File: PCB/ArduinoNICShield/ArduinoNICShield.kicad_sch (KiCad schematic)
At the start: 4 parts, among them J2 OUT, Q1 PN2222A

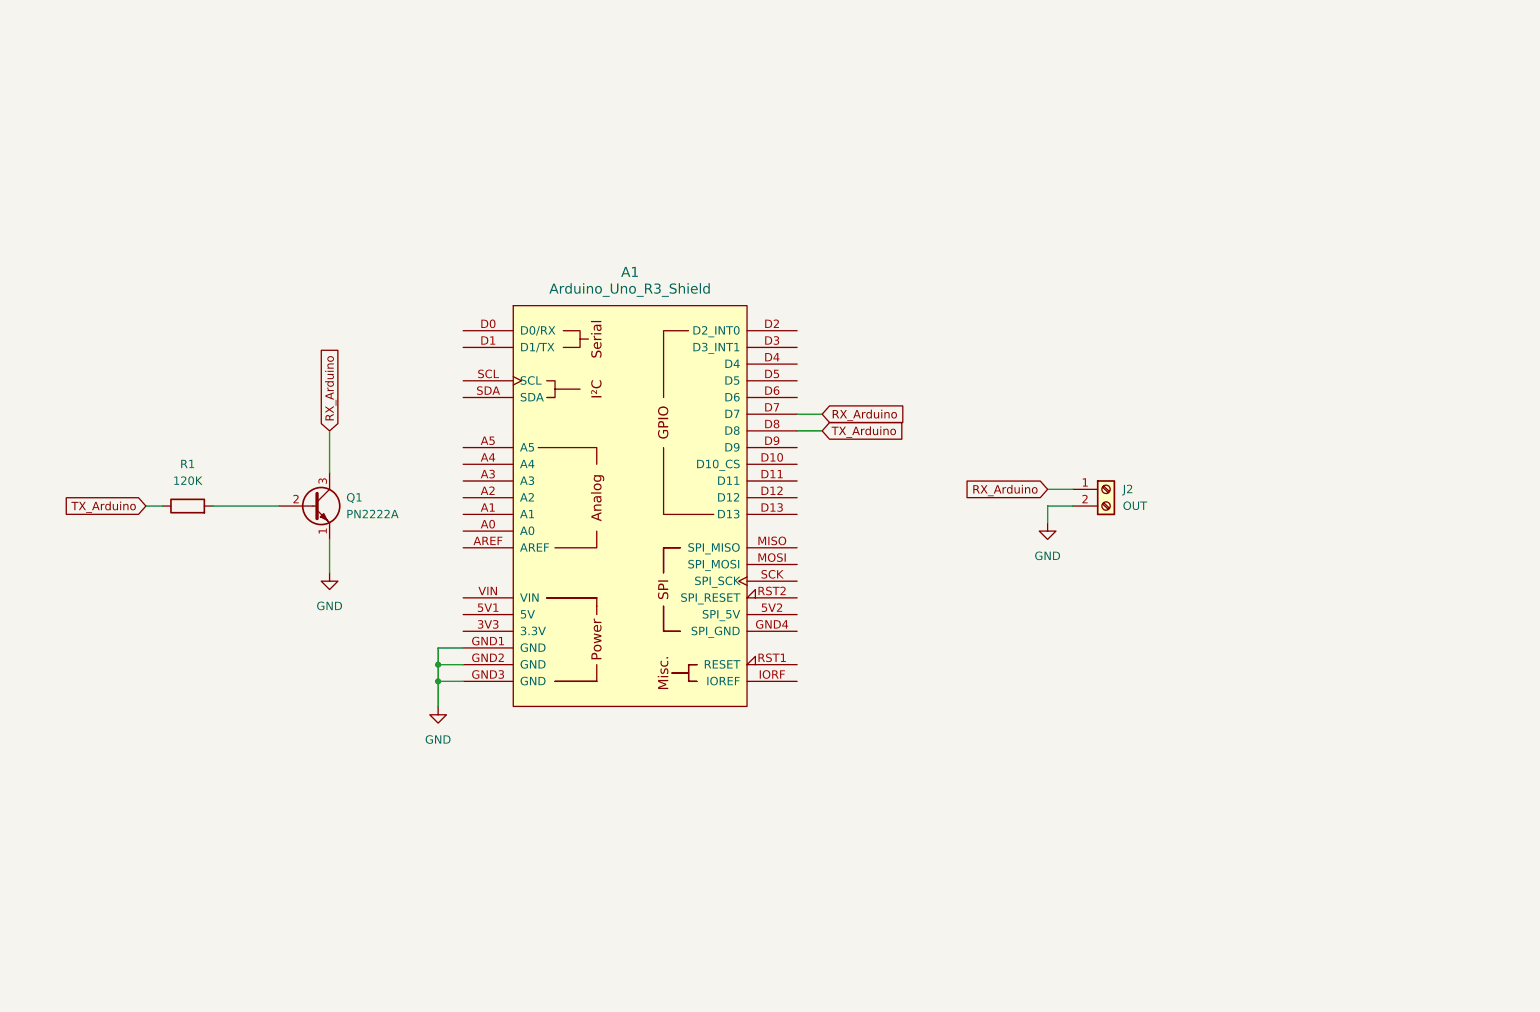
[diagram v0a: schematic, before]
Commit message: Correction of the arduino library, and start of the implementation of the python interface
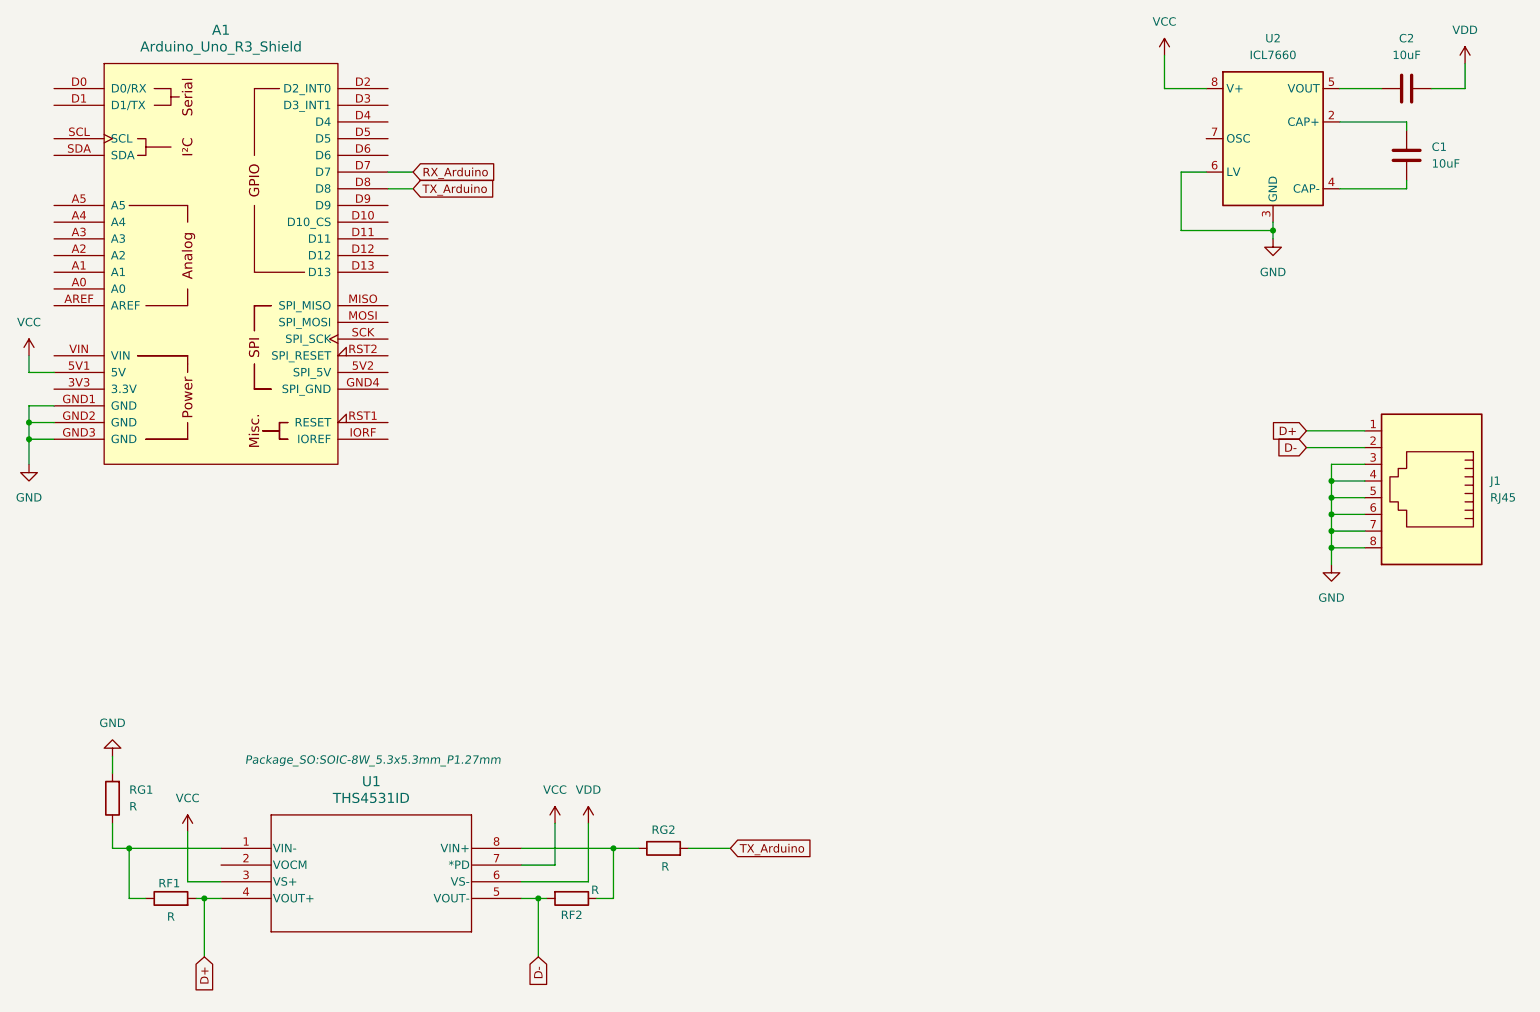
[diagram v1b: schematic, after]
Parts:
- removed J2: OUT, TerminalBlock:TerminalBlock_Xinya_XY308-2.54-2P_1x02_P2.54mm_Horizontal, symbol Connector:Screw_Terminal_01x02
- removed Q1: PN2222A, Package_TO_SOT_THT:TO-92_Inline, symbol Transistor_BJT:PN2222A
- removed R1: 120K, Resistor_SMD:R_1206_3216Metric_Pad1.30x1.75mm_HandSolder, symbol Device:R
- added C1, C2: 10uF, Capacitor_SMD:C_1206_3216Metric_Pad1.33x1.80mm_HandSolder, symbol Device:C
- added J1: RJ45, Connector_RJ:RJ45_Ninigi_GE, symbol Connector:RJ45
- added RF1, RF2, RG1, RG2: R, Resistor_SMD:R_1206_3216Metric_Pad1.30x1.75mm_HandSolder, symbol Device:R
- added U1: THS4531ID, Package_SO:SOIC-8W_5.3x5.3mm_P1.27mm, symbol THS4531:THS4531ID
- added U2: ICL7660, Package_SO:SOIC-8_5.23x5.23mm_P1.27mm, symbol Regulator_SwitchedCapacitor:ICL7660
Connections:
- net GND: now also J1.3, J1.4, J1.5, J1.6, J1.7, J1.8, RG1.2, U2.3 (GND), U2.6 (LV)
- net TX_Arduino: now also RG2.2
- net VCC: now reaches A1.5V1 (5V)
- net VCC: now also U1.3 (VS+), U1.7 (*PD), U2.8 (V+)
- new net: C1.1, U2.2 (CAP+)
- new net: C1.2, U2.4 (CAP-)
- new net: RF1.1, RG1.1, U1.1 (VIN-)
- new net: RF2.1, RG2.1, U1.8 (VIN+)
- new net: C2.1, U2.5 (VOUT)
- new net D+: J1.1, RF1.2, U1.4 (VOUT+)
- new net D-: J1.2, RF2.2, U1.5 (VOUT-)
- new net VDD: C2.2, U1.6 (VS-)
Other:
- moved on the sheet: A1
